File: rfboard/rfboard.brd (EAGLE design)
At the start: 30 x 60 mm, 34 parts, among them Q1 IRLML5203, Q2 IRLML5203, Q3 IRLML5203, Q4 IRLML5203, Q5 IRLML5203

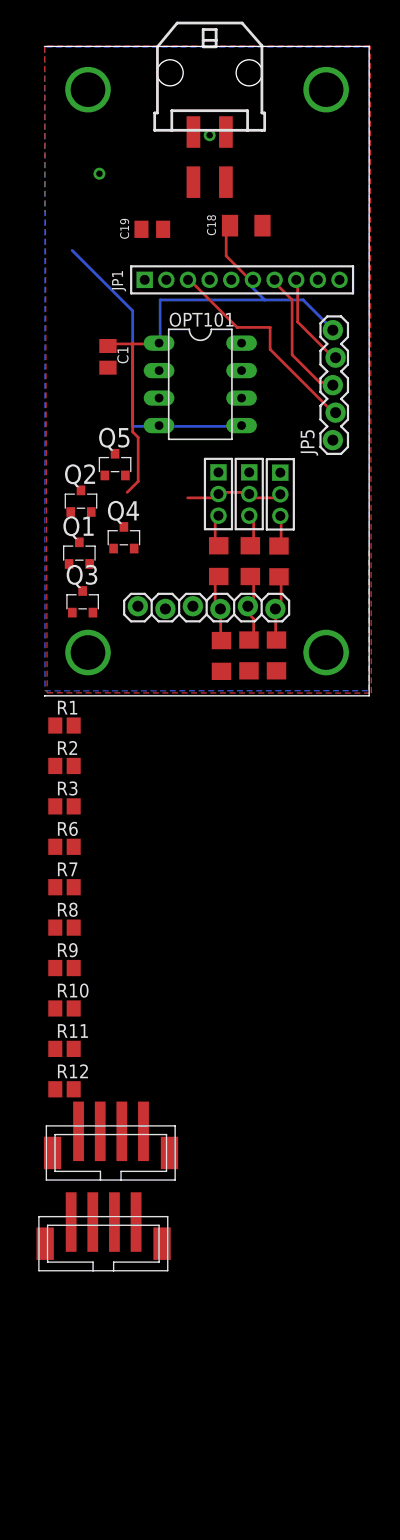
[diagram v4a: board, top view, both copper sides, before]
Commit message: Deleted voltage dividers, modified pinout
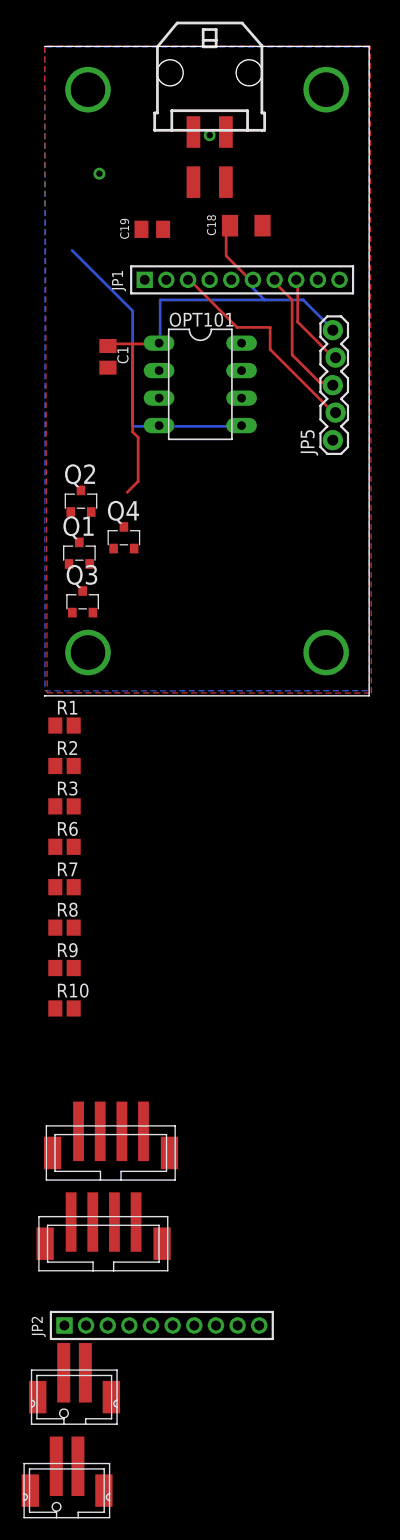
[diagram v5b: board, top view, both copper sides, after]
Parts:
- removed JP11, JP6, JP8: (no value), pinhead-2:1X03M
- removed JP4: (no value), SparkFun-Connectors:1X06_LOCK
- removed Q5: IRLML5203, ngohara_parts:MICRO3
- removed R11, R12: (no value), resistor:R0805
- removed R1A, R1B, R2A, R2B, R3A, R3B: (no value), rcl:R1206
- added JP2: (no value), pinhead-2:1X10M
- added LSM_PWR, U$2: JST-PH2-SMD, jst-ph:JST-PH2-SMD
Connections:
- removed net DATA1: JP6.3, R1A.2
- removed net DATA2: JP8.3, R2A.2
- removed net DATA3: JP11.3, R3A.2
- removed net N$11: Q5.3, R12.2
- removed net N$12: Q5.2, R11.2
- removed net N$13: R11.1
- removed net N$14: Q5.1, R12.1
- removed net VD1: JP4.1, R1A.1, R1B.2
- removed net VD2: JP4.2, R2A.1, R2B.2
- removed net VD3: JP4.3, R3A.1, R3B.2
- net 3.3V: no longer JP11.2, JP6.2, JP8.2
- net GND: no longer JP11.1, JP6.1, JP8.1, R1B.1, R2B.1, R3B.1
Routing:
- net 3.3V: track 57.1 -> 48.0 mm
- net VD2: track 6.73 -> 0.00 mm
- net VD3: track 6.45 -> 0.00 mm
- net VD1: track 6.12 -> 0.00 mm
- net DATA2: track 3.06 -> 0.00 mm
- net DATA3: track 3.01 -> 0.00 mm
- net DATA1: track 2.83 -> 0.00 mm

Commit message: added voltage div to Amb_out, and amb_on fet
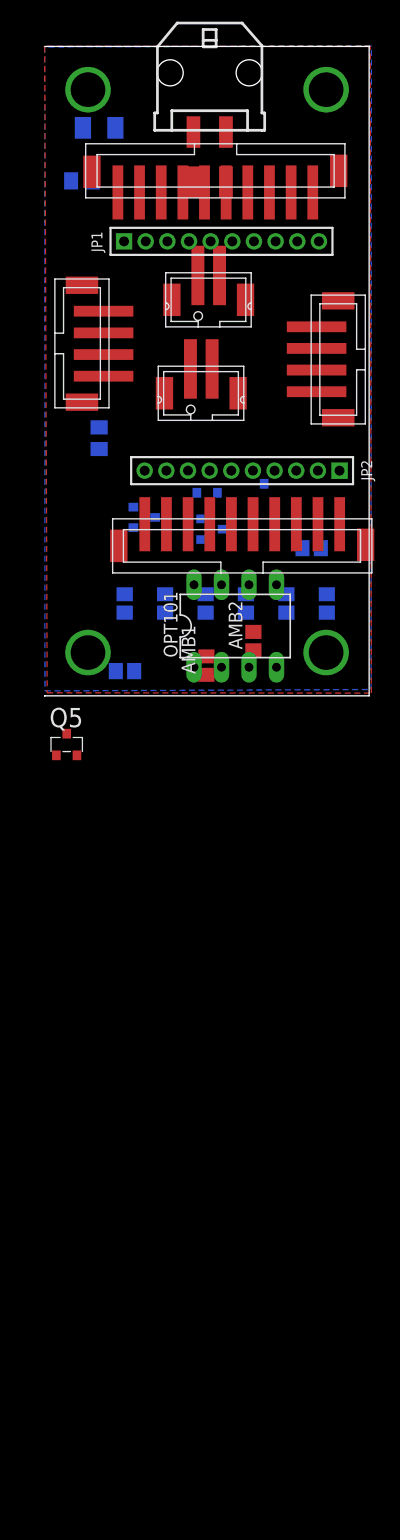
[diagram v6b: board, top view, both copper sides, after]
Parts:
- removed JP5: (no value), SparkFun-Connectors:1X05_LOCK
- added AMB1: 200k, resistor:R0805
- added AMB2: 96k, resistor:R0805
- added Q5: IRLML5203, ngohara_parts:MICRO3
- added U$1, U$3: JST-PH10-SMD, jst-ph:JST-PH10-SMD
- R1, R10, R2, R3, R6, R7, R8, R9: value (none) -> 10k
- moved LSM_PWR 102.1 mm to (11.2, 34.1)
- moved U$2 102.1 mm to (10.5, 25.5)
- moved 5V 83.8 mm to (29.6, 25.1), turned to 90 degrees
- moved 3.3V 83.2 mm to (0.94, 38.5), turned to 270 degrees
- moved JP2 79.3 mm to (18.2, 20.8), turned to 180 degrees
- moved R9 41.5 mm to (26.1, 8.53), flipped to the bottom, turned to 90 degrees
- moved R8 36.3 mm to (22.3, 8.53), flipped to the bottom, turned to 90 degrees
- moved R10 31.7 mm to (7.42, 2.29), flipped to the bottom
- moved R7 31.1 mm to (18.6, 8.53), flipped to the bottom, turned to 90 degrees
- moved R1 28.1 mm to (24.7, 13.6), flipped to the bottom
- moved R6 26.0 mm to (14.9, 8.53), flipped to the bottom, turned to 90 degrees
- moved OPT101 22.6 mm to (17.6, 6.45), turned to 0 degrees
- moved R3 20.9 mm to (11.1, 8.53), flipped to the bottom, turned to 90 degrees
- moved Q3 19.5 mm to (20.3, 18.6), flipped to the bottom
- moved C18 16.3 mm to (5.03, 52.5), flipped to the bottom
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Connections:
- removed net DIN: JP1.7, JP5.3
- new net AD0/DI0: JP2.1, U$1.P$10
- new net AD1/DI1: JP2.2, U$1.P$9
- new net AD2/DI2: JP2.3, U$1.P$8
- new net AD3/D13: JP2.4, U$1.P$7
- new net AD4/DI4: JP2.10, U$1.P$1
- new net AMB_LOW: AMB1.1, AMB2.1
- new net AMB_ON: Q5.1, U$2.P$1
- new net ASS/AD5/DI5: JP2.6, U$1.P$5
- new net CTS/DI7: JP2.9, U$1.P$2
- new net DIN/CONFIG: JP1.8, U$3.P$3
- new net DO8: JP1.7, U$3.P$4
- new net DTR/SLEEP_RQ/D18: JP1.2, U$3.P$9
- new net ON/SLEEP: JP2.8, U$1.P$3
- new net PWM0/RSSI: JP1.5, U$3.P$6
- new net PWM1: JP1.4, U$3.P$7
- new net RST/AD6/DI6: JP2.5, U$1.P$6
- new net VREF: JP2.7, U$1.P$4
- net 3.3V: now also JP1.10, Q5.3
- net 5V: now also LSM_PWR.P$1
- net AMB_OUT: now also AMB1.2
- net DOUT: now also JP1.9, U$3.P$2; no longer JP1.8, JP5.4
- net GND: now also AMB2.2, JP1.1, LSM_PWR.P$2
- net RESET: now also JP1.6, U$3.P$5; no longer JP1.3, JP5.2
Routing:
- net 3.3V: track 48.0 -> 0.00 mm
- net AMB_OUT: track 28.7 -> 0.00 mm
- net RESET: track 19.8 -> 0.00 mm
- net DIN: track 12.5 -> 0.00 mm
- net DOUT: track 8.74 -> 0.00 mm

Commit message: finished laying board with components on bottom
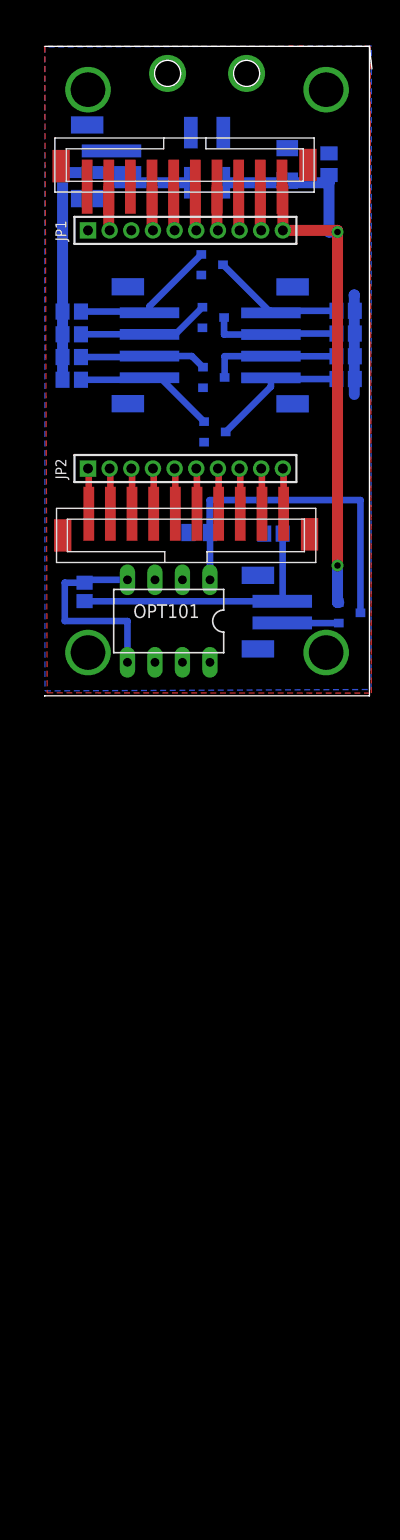
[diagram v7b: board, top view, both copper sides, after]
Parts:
- removed X2: (no value), con-molex-micro-fit-3_0:43045-0406
- added X1: (no value), con-molex-micro-fit-3_0:43045-0406
- moved R10 37.3 mm to (27.8, 33.5)
- moved R9 34.3 mm to (2.50, 33.4), turned to 180 degrees
- moved R2 33.9 mm to (27.8, 35.6), turned to 0 degrees
- moved R1 31.1 mm to (2.50, 35.5), turned to 180 degrees
- moved Q5 28.8 mm to (28.2, 7.67), flipped to the bottom, turned to 90 degrees
- moved R6 26.2 mm to (27.8, 31.4), turned to 0 degrees
- moved R7 26.2 mm to (2.50, 29.2), turned to 180 degrees
- moved 5V 24.5 mm to (5.18, 26.4), flipped to the bottom
- moved 3.3V 24.5 mm to (25.4, 38.4), flipped to the bottom
- moved Q1 24.4 mm to (15.5, 39.8)
- moved R3 24.3 mm to (2.50, 31.3), turned to 180 degrees
- moved C19 22.9 mm to (26.3, 49.1), turned to 90 degrees
- moved U$2 22.7 mm to (17.2, 3.76), flipped to the bottom, turned to 90 degrees
- moved R8 21.4 mm to (27.8, 29.3), turned to 0 degrees
- moved Q2 19.5 mm to (15.6, 35.0)
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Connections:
- new net VIN: C1.1, OPT101.1, Q5.3
- net 3.3V: now also Q5.2, U$3.P$1, X1.P$3; no longer C1.1, OPT101.1, Q5.3, X2.P$3
- net 5V: now also X1.P$4; no longer X2.P$4
- net AD0/DI0: now also U$1.P$1; no longer U$1.P$10
- net AD1/DI1: now also U$1.P$2; no longer U$1.P$9
- net AD2/DI2: now also U$1.P$3; no longer U$1.P$8
- net AD3/D13: now also U$1.P$4; no longer U$1.P$7
- net AD4/DI4: now also U$1.P$10; no longer U$1.P$1
- net AMB_LOW: now also U$2.P$2
- net ASS/AD5/DI5: now also U$1.P$6; no longer U$1.P$5
- net CTS/DI7: now also U$1.P$9; no longer U$1.P$2
- net GND: now also U$3.P$10, X1.P$1, X1.P$2; no longer X2.P$1, X2.P$2
- net H1: now also 5V.P$4; no longer 5V.P$1
- net H2: now also 5V.P$3; no longer 5V.P$2
- net H3: now also 5V.P$2; no longer 5V.P$3
- net H4: now also 5V.P$1; no longer 5V.P$4
- net ON/SLEEP: now also U$1.P$8; no longer U$1.P$3
- net RST/AD6/DI6: now also U$1.P$5; no longer U$1.P$6
- net VREF: now also U$1.P$7; no longer U$1.P$4
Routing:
- net 3.3V: track 0.00 -> 59.5 mm, vias 0 -> 2
- net 5V: track 0.00 -> 31.9 mm
- net VIN: track 0.00 -> 31.7 mm
- net AMB_LOW: track 0.00 -> 24.5 mm
- net AMB_OUT: track 0.00 -> 19.2 mm
- net H1: track 0.00 -> 13.8 mm
- net H4: track 0.00 -> 13.2 mm
- net L4: track 0.00 -> 12.9 mm
- net L1: track 0.00 -> 12.5 mm
- net L3: track 0.00 -> 12.3 mm
- net H2: track 0.00 -> 12.3 mm
- net L2: track 0.00 -> 12.0 mm
- net H3: track 0.00 -> 11.8 mm
- net N$1: track 0.00 -> 9.22 mm
- net AMB_ON: track 0.00 -> 5.23 mm
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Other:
- board size 30 x 60 mm -> 30.2 x 60 mm

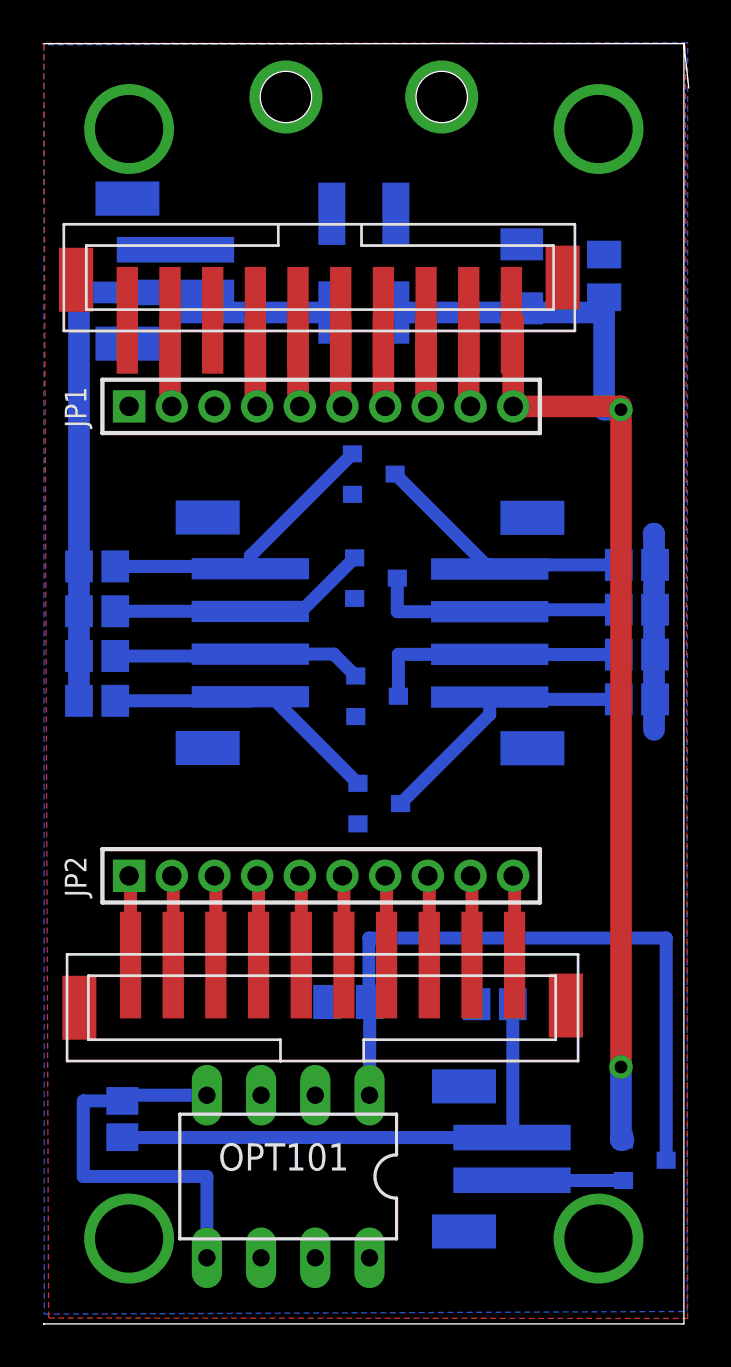
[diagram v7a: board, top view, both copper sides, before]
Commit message: Fixed fet Amb_On with resistors, fixed connector orientation, fixed text
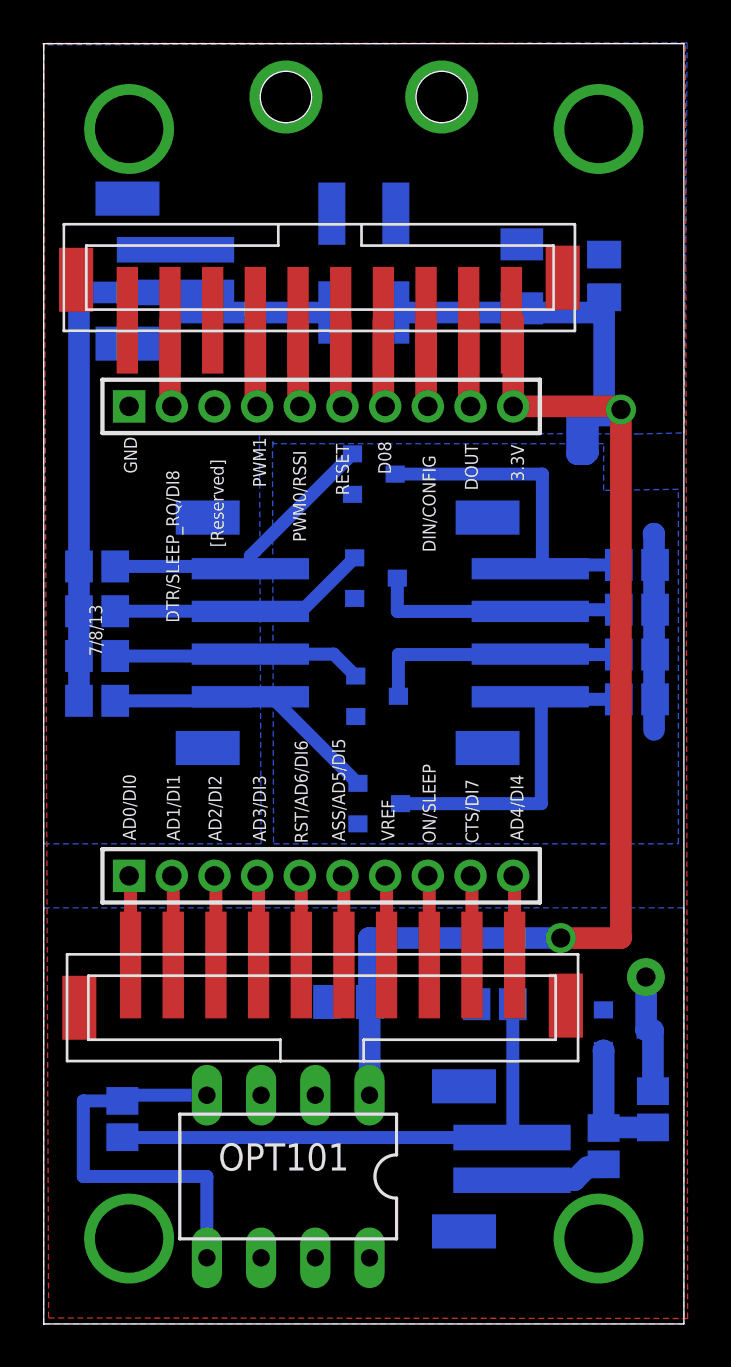
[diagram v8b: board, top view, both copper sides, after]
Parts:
- added RGS: 2.2k, resistor:R0805
- added RIN: 10k, resistor:R0805
- moved 3.3V 13.9 mm to (18.3, 26.4), turned to 90 degrees
- moved Q5 6.17 mm to (27.2, 13.8)
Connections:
- removed net VIN: C1.1, OPT101.1, Q5.3
- new net N$2: Q5.1, RGS.1, RIN.2
- new net N_GND: AMB2.2, C1.2, OPT101.3, OPT101.8, Q5.2
- net 3.3V: now also C1.1, OPT101.1, Q1.1, Q2.1, Q3.1, Q4.1, R10.1, R2.1, R6.1, R8.1; no longer Q5.2
- net AMB_ON: now also RIN.1; no longer Q5.1
- net GND: now also Q5.3, RGS.2; no longer AMB2.2, C1.2, OPT101.3, OPT101.8, Q1.1, Q2.1, Q3.1, Q4.1, R10.1, R2.1, R6.1, R8.1
- net L1: now also 3.3V.P$4; no longer 3.3V.P$1
- net L2: now also 3.3V.P$3; no longer 3.3V.P$2
- net L3: now also 3.3V.P$2; no longer 3.3V.P$3
- net L4: now also 3.3V.P$1; no longer 3.3V.P$4
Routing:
- net VIN: track 31.7 -> 0.00 mm
- net 3.3V: track 59.5 -> 84.0 mm
- net N$1: track 9.22 -> 0.00 mm
- net N$2: track 0.00 -> 5.96 mm
- net GND: track 0.00 -> 5.68 mm, vias 0 -> 1
- net L1: track 12.5 -> 15.5 mm
- net L4: track 12.9 -> 15.8 mm
- added copper zone on layer 16, net 3.3V
- added copper zone on layer 16, net N_GND
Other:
- board size 30.2 x 60 mm -> 30 x 60 mm
- board text added: "3.3 Out"
- board text added: "3.3V"
- board text added: "5V In"
- board text added: "7/8/13"
- board text added: "ABM_ON"
- board text added: "AD0/DI0"
- board text added: "AD1/DI1"
- board text added: "AD2/DI2"
- board text added: "AD3/DI3"
- board text added: "AD4/DI4"
- board text added: "AMB_OUT"
- board text added: "ASS/AD5/DI5"
- board text added: "CTS/DI7"
- board text added: "D08"
- board text added: "DIN/CONFIG"
- board text added: "DOUT"
- board text added: "DTR/SLEEP_RQ/DI8"
- board text added: "GND"
- board text added: "ON/SLEEP"
- board text added: "PWM0/RSSI"
- board text added: "PWM1"
- board text added: "RESET"
- board text added: "RST/AD6/DI6"
- board text added: "VREF"
- board text added: "[Reserved]"
